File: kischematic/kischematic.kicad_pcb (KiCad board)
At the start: 2 copper layers, 26.7 x 50 mm, 105 parts, among them IC1 BlueNRG, IC10 128x64OLED, IC11 BALF-BRG-01D3, IC12 MAX44009, IC2 EFM32ZG108, IC3 BQ297xx, IC4 AAT3672IWO-4.2-1, IC5 TPS6223xx, IC6 MAX44009, IC8 BSD840NH6327XTSA1, IC9 MMA8653FC, J1 0, J2 Screw_Terminal_1x01, J5 Screw_Terminal_1x01, J6 Screw_Terminal_1x01, P1 CONN_01X01, P2 CONN_01X01, P3 CONN_01X01, P4 CONN_01X01, P5 CONN_01X01, P6 CONN_01X01, P7 CONN_01X01, P8 CONN_01X04, P9 CONN_01X04, SW1 SW_Push, SW2 SW_Push, U1 USB-C, U2 SWD_SPRING, U3 FT200XD, Y1 32k, Y2 16M

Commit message: Tidying up.
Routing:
- net VREG: track 191.2 -> 178.7 mm
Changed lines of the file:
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@@
     (thickness 1.6)
     (drawings 223)
-    (tracks 2148)
+    (tracks 2132)
     (zones 0)
     (modules 105)
@@
   )
   (setup
-    (last_trace_width 0.1525)
+    (last_trace_width 0.5)
     (user_trace_width 0.16)
     (user_trace_width 0.2)
@@
   (segment (start 87.29 68.86) (end 87.3 68.85) (width 0.29) (layer B.Cu) (net 0))
   (segment (start 93.5 31.79) (end 93.61 31.68) (width 0.29) (layer B.Cu) (net 0))
+  (segment (start 91.1 27.2) (end 91.1 25.91) (width 0.29) (layer B.Cu) (net 1))
   (via (at 86.76 40.78) (size 0.7) (drill 0.35) (layers F.Cu B.Cu) (net 1))
   (segment (start 86.76 40.78) (end 86.94 40.96) (width 0.29) (layer F.Cu) (net 1))
@@
   (segment (start 91.6 27.2) (end 91.6 25.73) (width 0.29) (layer B.Cu) (net 1))
   (segment (start 91.1 25.91) (end 90.87 25.68) (width 0.29) (layer B.Cu) (net 1))
-  (segment (start 91.1 27.2) (end 91.1 25.91) (width 0.29) (layer B.Cu) (net 1))
   (segment (start 96.6 28.8) (end 96.49 28.91) (width 0.2) (layer B.Cu) (net 1))
   (segment (start 96.49 28.91) (end 95.57 28.91) (width 0.2) (layer B.Cu) (net 1))
@@
   (segment (start 94 47) (end 94.71 46.29) (width 0.2) (layer F.Cu) (net 1) (status 30))
   (segment (start 94 47) (end 95 48) (width 0.2) (layer F.Cu) (net 1) (status 30))
+  (segment (start 94.74 26.63) (end 94.753 26.643) (width 0.5) (layer F.Cu) (net 2))
+  (segment (start 94.753 26.643) (end 94.753 28.267) (width 0.5) (layer F.Cu) (net 2))
+  (segment (start 94.753 28.267) (end 94.27 28.75) (width 0.5) (layer F.Cu) (net 2))
+  (segment (start 82.77 26.63) (end 94.74 26.63) (width 0.5) (layer F.Cu) (net 2))
+  (segment (start 94.74 26.63) (end 101.63 26.63) (width 0.5) (layer F.Cu) (net 2))
+  (segment (start 81.24 27.01) (end 82.4 27) (width 0.5) (layer F.Cu) (net 2))
+  (segment (start 82.4 27) (end 82.77 26.63) (width 0.5) (layer F.Cu) (net 2))
+  (segment (start 101.63 26.63) (end 102.15 27.15) (width 0.5) (layer F.Cu) (net 2))
+  (segment (start 102.15 27.15) (end 102.15 28.4) (width 0.5) (layer F.Cu) (net 2))
+  (segment (start 102.15 28.4) (end 102.15 31.21) (width 0.5) (layer F.Cu) (net 2))
   (via (at 94.27 28.75) (size 0.62) (drill 0.31) (layers F.Cu B.Cu) (net 2))
-  (segment (start 94.12 28.9) (end 93.7 28.9) (width 0.29) (layer F.Cu) (net 2))
   (segment (start 96.61 42.12) (end 96.45 41.96) (width 0.42) (layer F.Cu) (net 2))
   (segment (start 96.45 41.66) (end 95.545 40.755) (width 0.42) (layer F.Cu) (net 2))
@@
   (segment (start 85.35 62.22) (end 86.5 61.07) (width 0.29) (layer F.Cu) (net 2))
   (segment (start 86.5 61.07) (end 86.5 60.75) (width 0.29) (layer F.Cu) (net 2))
-  (segment (start 100.16 28.87) (end 100.16 28.474) (width 0.5) (layer F.Cu) (net 2))
-  (segment (start 100.354 28.28) (end 102.03 28.28) (width 0.5) (layer F.Cu) (net 2))
-  (segment (start 100.16 28.474) (end 100.354 28.28) (width 0.5) (layer F.Cu) (net 2))
-  (segment (start 102.03 28.28) (end 102.15 28.4) (width 0.5) (layer F.Cu) (net 2))
-  (segment (start 102.15 28.4) (end 102.15 31.21) (width 0.5) (layer F.Cu) (net 2))
   (segment (start 92.15 42.67) (end 92.15 42.65) (width 0.5) (layer F.Cu) (net 2))
   (segment (start 88.52 68.32) (end 89.93 68.32) (width 0.2) (layer F.Cu) (net 2))
@@
   (segment (start 81.24 27.01) (end 78.07 27.01) (width 0.5) (layer B.Cu) (net 2))
   (segment (start 78.07 27.01) (end 77.83 27.25) (width 0.5) (layer B.Cu) (net 2))
-  (segment (start 89.94 27) (end 81.25 27) (width 0.5) (layer F.Cu) (net 2))
   (segment (start 81.25 27) (end 81.24 27.01) (width 0.5) (layer F.Cu) (net 2))
   (via (at 77.83 27.25) (size 0.7) (drill 0.35) (layers F.Cu B.Cu) (net 2))
@@
   (segment (start 96.537957 47.997577) (end 96.537957 48.017957) (width 0.2) (layer F.Cu) (net 2))
   (segment (start 98.18 48.45) (end 98.18 48.9) (width 0.2) (layer F.Cu) (net 2) (status 10))
-  (segment (start 94.27 28.75) (end 94.12 28.9) (width 0.29) (layer F.Cu) (net 2))
   (segment (start 94.1 27.2) (end 94.1 28.58) (width 0.29) (layer B.Cu) (net 2))
   (segment (start 94.1 28.58) (end 94.27 28.75) (width 0.29) (layer B.Cu) (net 2))
@@
   (segment (start 97.1 39.8) (end 97.475 39.8) (width 0.2) (layer F.Cu) (net 2))
   (segment (start 90.087818 46.91) (end 90.388909 47.211091) (width 0.29) (layer F.Cu) (net 2))
-  (segment (start 82.4 27) (end 89.94 27) (width 0.5) (layer F.Cu) (net 2))
-  (segment (start 92.6 26.94) (end 92.54 27) (width 0.29) (layer F.Cu) (net 2))
-  (segment (start 89.94 27) (end 92.54 27) (width 0.5) (layer F.Cu) (net 2))
-  (segment (start 89.84 26.9) (end 89.94 27) (width 0.29) (layer F.Cu) (net 2))
-  (segment (start 94.801 27) (end 98.528 27) (width 0.5) (layer F.Cu) (net 2))
-  (segment (start 89.94 27) (end 94.801 27) (width 0.5) (layer F.Cu) (net 2))
-  (segment (start 98.9 27.372) (end 98.528 27) (width 0.5) (layer F.Cu) (net 2))
-  (segment (start 95.13 27.329) (end 94.801 27) (width 0.5) (layer F.Cu) (net 2))
   (segment (start 92.57 25.62) (end 92.6 25.59) (width 0.29) (layer B.Cu) (net 2))
   (segment (start 93.52 25.59) (end 92.6 25.59) (width 0.2) (layer B.Cu) (net 2))
@@
   (segment (start 98.12 49.99) (end 98.33 50.2) (width 0.2) (layer F.Cu) (net 2) (status 30))
   (segment (start 98.18 48.9) (end 98.12 48.96) (width 0.2) (layer F.Cu) (net 2))
-  (segment (start 98.9 28.9) (end 100.13 28.9) (width 0.5) (layer F.Cu) (net 2) (status 30))
-  (segment (start 100.13 28.9) (end 100.16 28.87) (width 0.5) (layer F.Cu) (net 2) (status 30))
-  (segment (start 98.9 28.9) (end 98.9 27.372) (width 0.5) (layer F.Cu) (net 2) (status 10))
-  (segment (start 95.13 27.84) (end 95.13 27.329) (width 0.5) (layer F.Cu) (net 2) (status 10))
-  (segment (start 93.7 28.893) (end 94.753 27.84) (width 0.5) (layer F.Cu) (net 2) (status 10))
-  (segment (start 94.753 27.84) (end 95.13 27.84) (width 0.5) (layer F.Cu) (net 2) (status 20))
-  (segment (start 93.7 28.9) (end 93.7 28.893) (width 0.5) (layer F.Cu) (net 2) (status 30))
   (segment (start 94.1 27.2) (end 94.1 26.17) (width 0.2) (layer B.Cu) (net 2) (status 10))
   (segment (start 92.6 27.2) (end 92.6 25.59) (width 0.29) (layer B.Cu) (net 2) (status 10))
@@
   (via (at 86.5 65.75) (size 0.7) (drill 0.35) (layers F.Cu B.Cu) (net 2))
   (segment (start 79.05 65.25) (end 79.28 65.02) (width 0.25) (layer F.Cu) (net 2))
-  (segment (start 93.7 28.9) (end 93.7 28.92) (width 0.2) (layer F.Cu) (net 2) (status 30))
-  (segment (start 94 28.6) (end 93.7 28.9) (width 0.5) (layer F.Cu) (net 2) (status 30))
   (segment (start 77.84 28.59) (end 76.94 29.49) (width 0.5) (layer F.Cu) (net 2) (status 10))
   (segment (start 76.94 31.315) (end 77.675 32.05) (width 0.5) (layer F.Cu) (net 2) (status 20))
@@
   (segment (start 101.76 25.79) (end 101.9 25.65) (width 0.2) (layer F.Cu) (net 71))
   (via (at 101.9 25.65) (size 0.62) (drill 0.31) (layers F.Cu B.Cu) (net 71))
-  (segment (start 99.86 26.06) (end 99.63 25.83) (width 0.2) (layer B.Cu) (net 72))
-  (segment (start 99.63 25.83) (end 96.42 25.83) (width 0.2) (layer B.Cu) (net 72))
+  (via (at 99.57 25.79) (size 0.62) (drill 0.31) (layers F.Cu B.Cu) (net 72))
+  (segment (start 99.57 25.79) (end 99.53 25.83) (width 0.2) (layer B.Cu) (net 72))
+  (segment (start 99.53 25.83) (end 96.42 25.83) (width 0.2) (layer B.Cu) (net 72))
   (segment (start 96.42 25.83) (end 96.13 26.12) (width 0.2) (layer B.Cu) (net 72))
-  (segment (start 96.13 26.12) (end 96.13 27.17) (width 0.2) (layer B.Cu) (net 72) (status 20))
+  (segment (start 96.13 26.12) (end 96.13 27.17) (width 0.2) (layer B.Cu) (net 72))
+  (segment (start 99.57 25.79) (end 100.16 25.79) (width 0.16) (layer F.Cu) (net 72))
   (segment (start 96.13 27.17) (end 96.1 27.2) (width 0.16) (layer B.Cu) (net 72) (status 30))
-  (segment (start 100.16 25.79) (end 100.13 25.79) (width 0.16) (layer F.Cu) (net 72) (status 30))
-  (segment (start 100.13 25.79) (end 99.86 26.06) (width 0.16) (layer F.Cu) (net 72) (status 10))
-  (via (at 99.86 26.06) (size 0.62) (drill 0.31) (layers F.Cu B.Cu) (net 72))
   (segment (start 83.38 25.67) (end 83.38 25.58) (width 0.29) (layer F.Cu) (net 73) (status 30))
   (segment (start 83.59 25.88) (end 83.38 25.67) (width 0.29) (layer F.Cu) (net 73) (status 20))

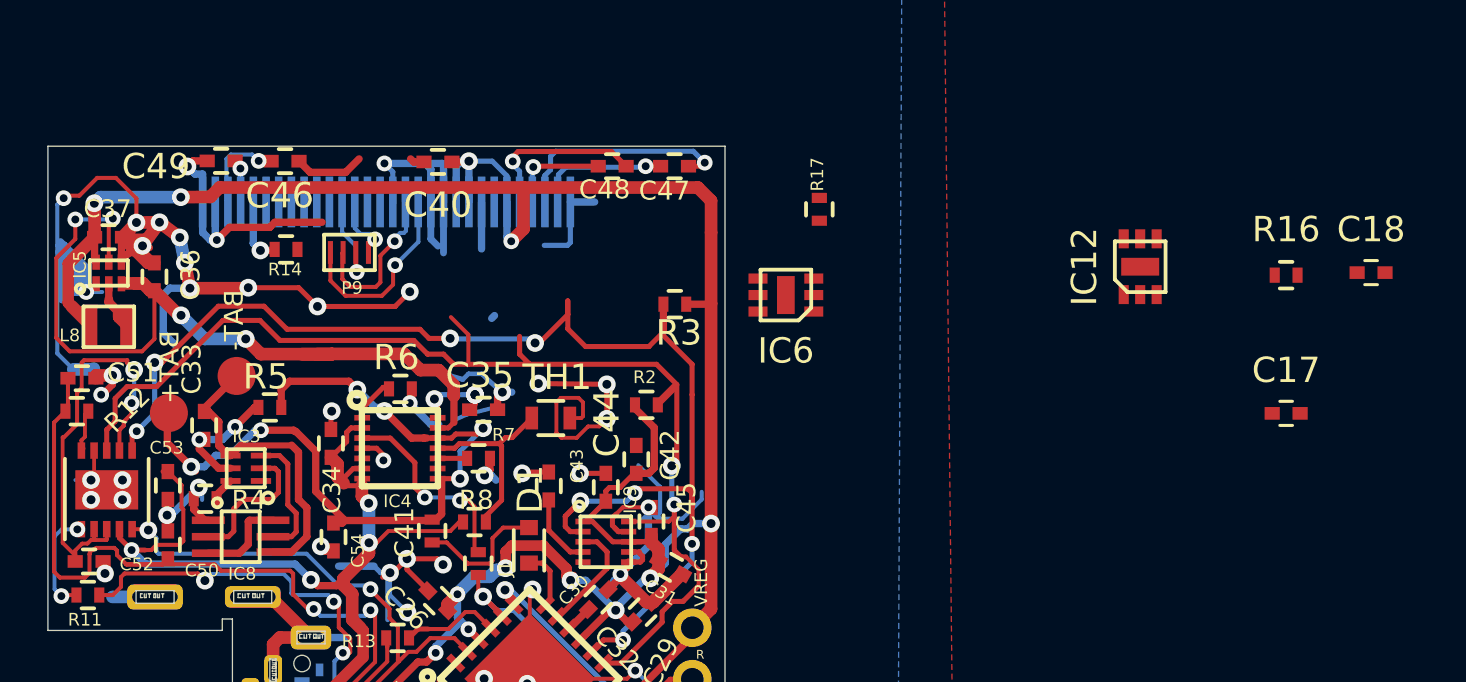
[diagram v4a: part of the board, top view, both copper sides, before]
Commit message: Some work on pcb layout for new sensors.
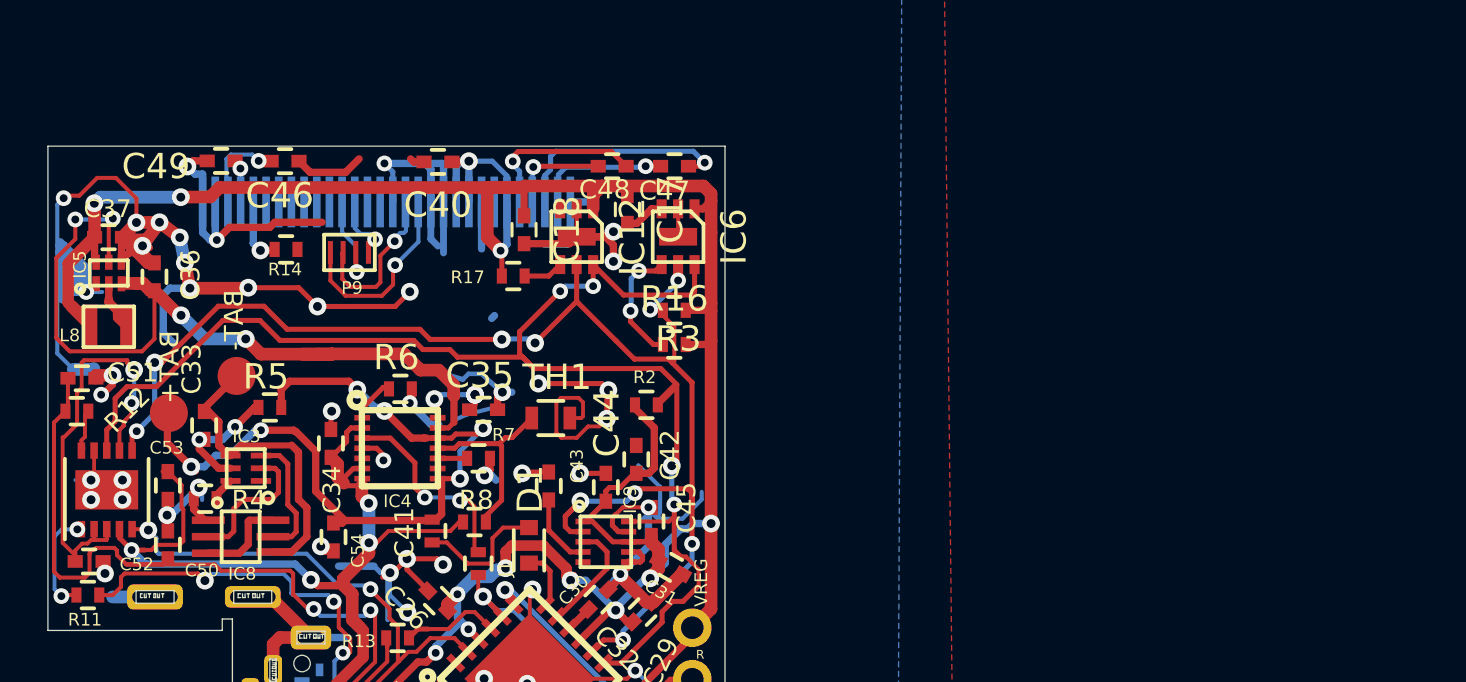
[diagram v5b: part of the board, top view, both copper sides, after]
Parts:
- moved C18 33.4 mm to (94.8, 28.3), turned to 270 degrees
- moved C17 27.2 mm to (98.8, 27.5), turned to 270 degrees
- moved R16 24.3 mm to (100.7, 32.8)
- moved IC12 22.3 mm to (96.8, 28.6), turned to 180 degrees
- moved R17 12.4 mm to (94.3, 30.1), turned to 180 degrees
- moved IC6 4.83 mm to (100.8, 28.6), turned to 180 degrees
- moved R3 0.24 mm to (100.7, 31.5)
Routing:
- net GND: track 414.5 -> 424.2 mm, vias 147 -> 149
- net I2C_SDA: track 47.4 -> 55.6 mm, vias 2 -> 4
- net VREG: track 178.7 -> 186.8 mm
- net Net-(IC6-Pad4): track 0.00 -> 4.96 mm, vias 0 -> 2
- net I2C_SCL: track 52.4 -> 56.2 mm, vias 8 -> 10
- net Net-(IC12-Pad4): track 0.00 -> 1.59 mm

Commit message: Minor.
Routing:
- net GND: track 424.2 -> 426.5 mm
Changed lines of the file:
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@@
     (thickness 1.6)
     (drawings 223)
-    (tracks 2202)
+    (tracks 2205)
     (zones 0)
     (modules 105)
@@
   )
   (setup
-    (last_trace_width 0.29)
+    (last_trace_width 0.16)
     (user_trace_width 0.16)
     (user_trace_width 0.2)
@@
   (segment (start 87.29 68.86) (end 87.3 68.85) (width 0.29) (layer B.Cu) (net 0))
   (segment (start 93.5 31.79) (end 93.61 31.68) (width 0.29) (layer B.Cu) (net 0))
-  (segment (start 99.8 27.47) (end 99.225 28.045) (width 0.29) (layer F.Cu) (net 1))
-  (segment (start 99.225 28.045) (end 98.85 28.045) (width 0.29) (layer F.Cu) (net 1))
-  (segment (start 100.2 27.47) (end 99.8 27.47) (width 0.29) (layer F.Cu) (net 1))
+  (segment (start 99.95 27.47) (end 99.375 28.045) (width 0.16) (layer F.Cu) (net 1))
+  (segment (start 99.375 28.045) (end 98.85 28.045) (width 0.16) (layer F.Cu) (net 1))
+  (segment (start 100.2 27.47) (end 99.95 27.47) (width 0.16) (layer F.Cu) (net 1))
+  (segment (start 98.85 28.17) (end 99.25 28.57) (width 0.29) (layer F.Cu) (net 1))
+  (segment (start 99.25 28.57) (end 100.85 28.57) (width 0.29) (layer F.Cu) (net 1))
+  (segment (start 98.85 28.045) (end 98.85 28.17) (width 0.29) (layer F.Cu) (net 1))
   (via (at 98.3 28.37) (size 0.7) (drill 0.35) (layers F.Cu B.Cu) (net 1))
   (segment (start 98.3 28.37) (end 98.15 28.37) (width 0.29) (layer F.Cu) (net 1))
